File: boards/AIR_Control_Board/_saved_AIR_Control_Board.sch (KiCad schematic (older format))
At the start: 77 parts, among them IC1 ATMEGA16M1, J1 AIR-, J2 Ultrafit_2, J3 To Interface Board, J4 PrechargeRelay, J5 AIR+, J6 CONN_02X03, Q2 NMOS_GSD_30V, Q3 NMOS_GSD_30V, Q4 NMOS_GSD_30V, Q5 NMOS_GSD_30V, Q6 NMOS_GSD_30V, Q7 NMOS_GSD_30V, U1 CAN_Transceiver, U2 TPS561201, Y1 Crystal_SMD

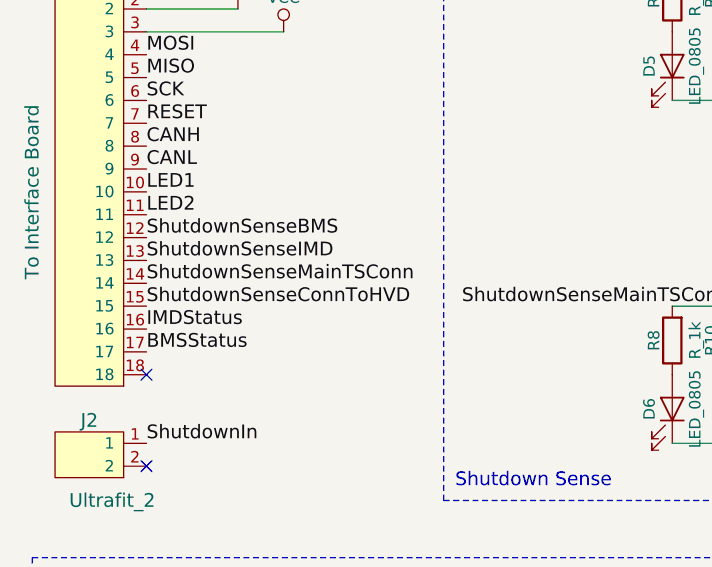
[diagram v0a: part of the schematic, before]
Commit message: finished layout for air ctrl board, starting tracing
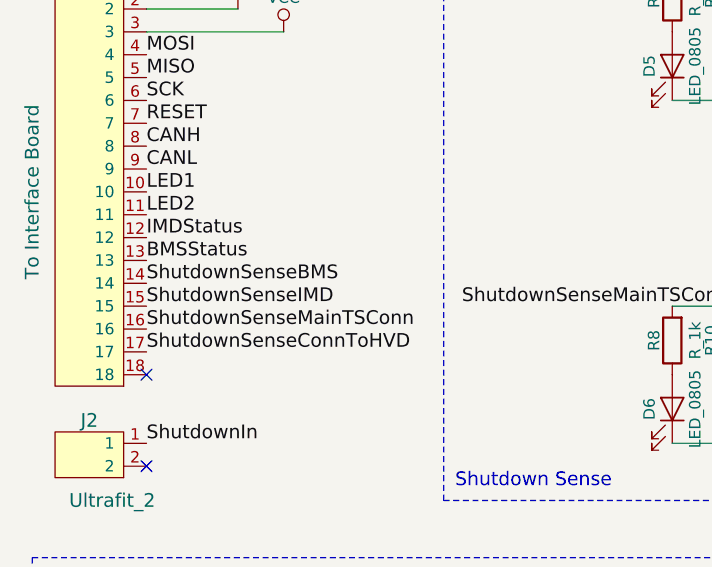
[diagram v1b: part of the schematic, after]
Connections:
- net BMSStatus: now also J3.13; no longer J3.17
- net IMDStatus: now also J3.12; no longer J3.16
- net ShutdownSenseBMS: now also J3.14; no longer J3.12
- net ShutdownSenseConnToHVD: now also J3.17; no longer J3.15
- net ShutdownSenseIMD: now also J3.15; no longer J3.13
- net ShutdownSenseMainTSConn: now also J3.16; no longer J3.14
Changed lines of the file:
@@
 Text Notes 700  4050 0    60   ~ 0
 To Relays
-Text Label 1150 2700 0    60   ~ 0
+Text Label 1150 2900 0    60   ~ 0
 ShutdownSenseMainTSConn
-Text Label 1150 2600 0    60   ~ 0
+Text Label 1150 2800 0    60   ~ 0
 ShutdownSenseIMD
 Text Label 3700 1300 2    60   ~ 0
 ShutdownSenseConnToHVD
-Text Label 1150 2500 0    60   ~ 0
+Text Label 1150 2700 0    60   ~ 0
 ShutdownSenseBMS
 Wire Wire Line
@@
 Wire Wire Line
 	1150 1600 1750 1600
-Text Label 1150 2900 0    60   ~ 0
+Text Label 1150 2500 0    60   ~ 0
 IMDStatus
-Text Label 1150 3000 0    60   ~ 0
+Text Label 1150 2600 0    60   ~ 0
 BMSStatus
 Text Label 9050 3500 0    60   ~ 0
@@
 	1    0    0    -1
 $EndComp
-Text Label 1150 2800 0    60   ~ 0
+Text Label 1150 3000 0    60   ~ 0
 ShutdownSenseConnToHVD
 Wire Wire Line
